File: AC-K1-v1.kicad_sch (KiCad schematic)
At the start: 169 parts, among them J1 S2B-PH-K-SLFSN, SW1 ESC, SW10 A, SW11 BSLH, SW12 LCMD, SW13 F2, SW14 2, SW15 W, SW16 S, SW17 Z, SW18 LALT, SW19 F3, SW2 GRAVE, SW20 3, SW21 E, SW22 D, SW23 X, SW24 F4, SW25 4, SW26 R, SW27 F, SW28 C, SW29 5, SW3 TAB, SW30 T, SW31 G, SW32 V, SW33 F5, SW34 6, SW35 Y, SW36 H, SW37 B, SW38 SPACE, SW39 F6, SW4 LCTRL, SW40 7, SW41 U, SW42 J, SW43 N, SW44 F7, SW45 8, SW46 I, SW47 K, SW48 M, SW49 F8, SW5 LSHIFT, SW50 9, SW51 O, SW52 L, SW53 COMMA, SW54 RALT, SW55 F9, SW56 0, SW57 P, SW58 SEMI, SW59 DOT, SW6 LCTRL, SW60 FN, SW61 F10, SW62 MINUS, SW63 LBKT, SW64 SQT, SW65 FSLH, SW66 RCTRL, SW67 F11, SW68 EQUAL, SW69 RBKT, SW7 F1, SW70 NUHS, SW71 RSHFT, SW72 LEFT, SW73 F12, SW74 BSPC, SW75 ENTER, SW76 UP, SW77 DOWN, SW78 DEL, SW79 HOME, SW8 1, SW80 PG_UP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

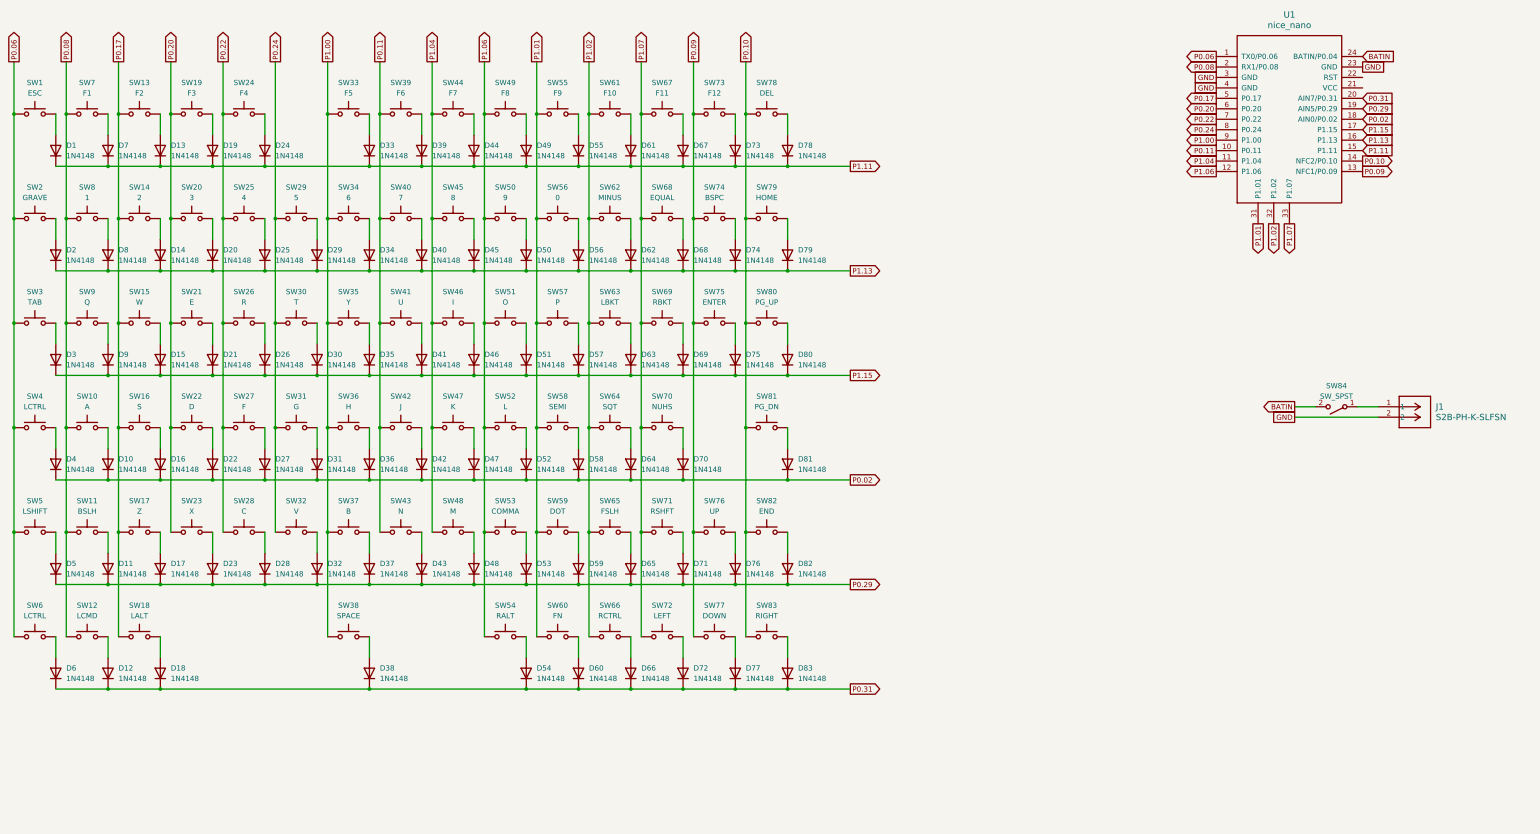
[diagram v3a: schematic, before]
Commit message: Added spacings to keycaps for easier alignment
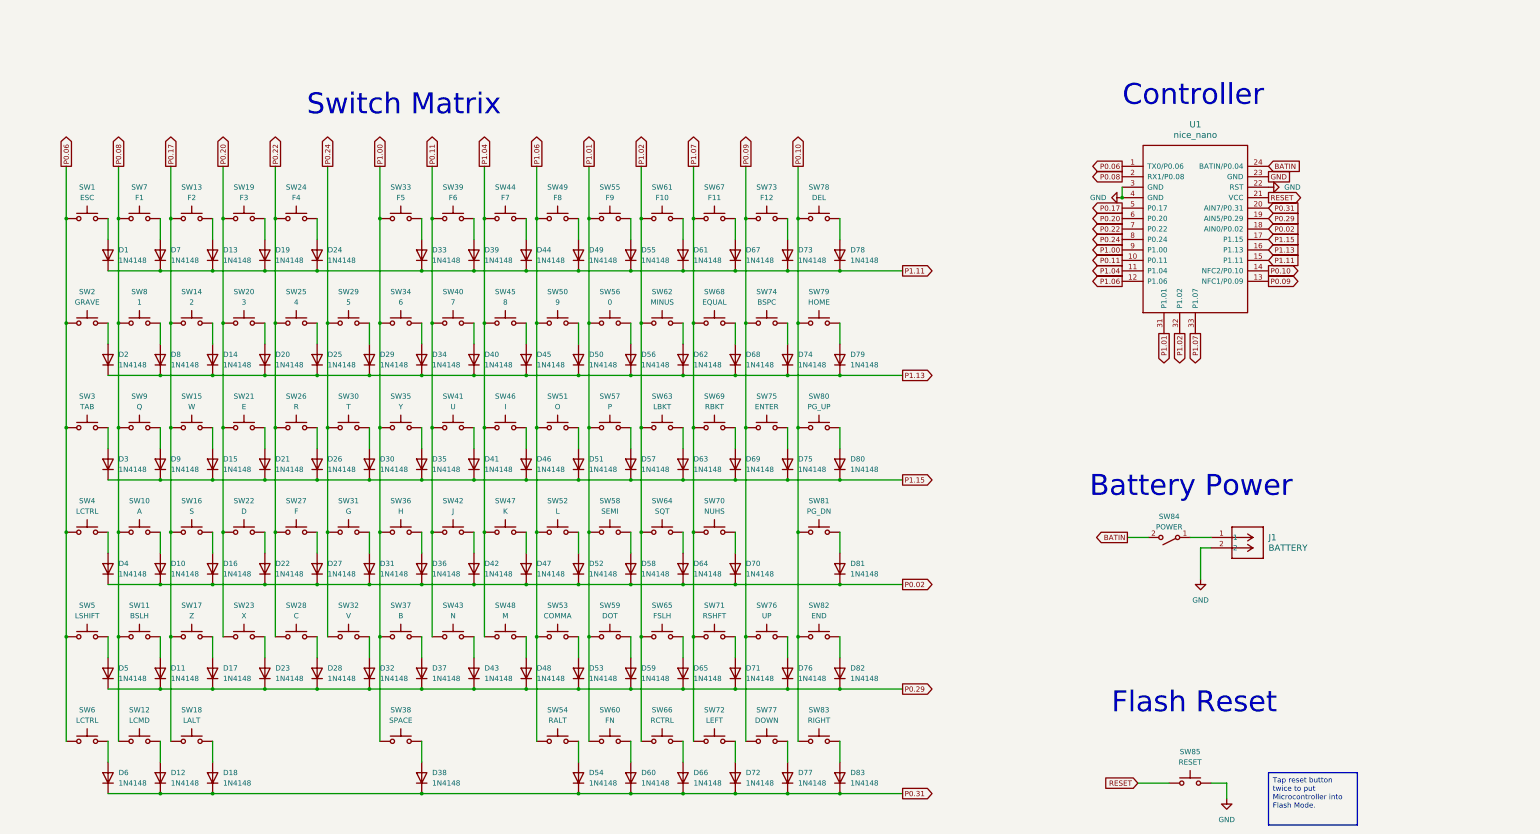
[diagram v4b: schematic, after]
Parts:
- added SW85: RESET, Button_Switch_THT:SW_PUSH_1P1T_6x3.5mm_H4.3_APEM_MJTP1243, symbol Switch:SW_Push
- J1: value S2B-PH-K-SLFSN -> BATTERY
- SW1, SW10, SW11, SW13, SW14, SW15, SW16, SW17, SW19, SW2, SW20, SW21, SW22, SW23, SW24, SW25, SW26, SW27, SW28, SW29, SW30, SW31, SW32, SW33, SW34, SW35, SW36, SW37, SW39, SW40, SW41, SW42, SW43, SW44, SW45, SW46, SW47, SW48, SW49, SW50, SW51, SW52, SW53, SW55, SW56, SW57, SW58, SW59, SW61, SW62, SW63, SW64, SW65, SW67, SW68, SW69, SW7, SW70, SW72, SW73, SW74, SW76, SW77, SW78, SW79, SW8, SW80, SW81, SW82, SW83, SW9: footprint marbastlib-choc:SW_choc_v1_1u -> Switch_Keyboard_Kailh:SW_Kailh_Choc_V1_1.00u_Spacing
- SW12, SW18, SW54, SW60, SW66: footprint marbastlib-choc:SW_choc_v1_1.25u -> Switch_Keyboard_Kailh:SW_Kailh_Choc_V1_1.25u_Spacing
- SW3: footprint marbastlib-choc:SW_choc_v1_1.5u -> Switch_Keyboard_Kailh:SW_Kailh_Choc_V1_1.50u_Spacing
- SW38: footprint Switch_Keyboard_Kailh:SW_Kailh_Choc_V1_6.00u -> Switch_Keyboard_Kailh:SW_Kailh_Choc_V1_6.00u_Spacing
- SW4: footprint marbastlib-choc:SW_choc_v1_1.75u -> Switch_Keyboard_Kailh:SW_Kailh_Choc_V1_1.75u_Spacing
- SW5, SW6: footprint marbastlib-choc:SW_choc_v1_1.25u -> Switch_Keyboard_Kailh:SW_Kailh_Choc_V1_1.50u_Spacing
- SW71: footprint marbastlib-choc:SW_choc_v1_1.75u -> Switch_Keyboard_Kailh:SW_Kailh_Choc_V1_1.00u_Spacing
- SW75: footprint Switch_Keyboard_Kailh:SW_Kailh_Choc_V1_ISOEnter -> Switch_Keyboard_Kailh:SW_Kailh_Choc_V1_ISOEnter_Spacing
- SW84: value SW_SPST -> POWER
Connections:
- net GND: now also U1.22 (RST), SW85.2
- net RESET: now reaches U1.21 (VCC)
- net RESET: now also SW85.1
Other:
- note added: "Battery Power"
- note added: "Controller"
- note added: "Flash Reset"
- note added: "Switch Matrix"
- moved on the sheet: D1, D10, D11, D12, D13, D14, D15, D16, D17, D18, D19, D2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

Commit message: Finished positioning switches
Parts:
- SW71: footprint Switch_Keyboard_Kailh:SW_Kailh_Choc_V1_1.00u_Spacing -> Switch_Keyboard_Kailh:SW_Kailh_Choc_V1_1.50u_Spacing
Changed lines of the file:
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@@
 			)
 		)
-		(property "Footprint" "Switch_Keyboard_Kailh:SW_Kailh_Choc_V1_1.00u_Spacing"
+		(property "Footprint" "Switch_Keyboard_Kailh:SW_Kailh_Choc_V1_1.50u_Spacing"
 			(at 208.28 172.72 0)
 			(effects

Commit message: Started pulling lanes
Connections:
- net GND: no longer U1.22 (RST)
- net RESET: now also U1.22 (RST); no longer U1.21 (VCC)
- no-connect marks 0 -> 1
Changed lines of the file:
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@@
 		(color 0 0 0 0)
 	)
+	(no_connect
+		(at 342.9 71.12)
+	)
 	(wire
 		(pts
@@
 	(global_label "RESET"
 		(shape output)
-		(at 342.9 71.12 0)
+		(at 342.9 68.58 0)
 		(fields_autoplaced yes)
 		(effects
@@
 		)
 		(property "Intersheetrefs" "${INTERSHEET_REFS}"
-			(at 351.6303 71.12 0)
+			(at 351.6303 68.58 0)
 			(effects
 				(font
@@
 		)
 	)
-	(global_label "GND"
-		(shape passive)
-		(at 342.9 66.04 0)
-		(fields_autoplaced yes)
-		(effects
-			(font
-				(size 1.27 1.27)
-			)
-			(justify left)
-		)
-		(property "Intersheetrefs" "${INTERSHEET_REFS}"
-			(at 348.6444 66.04 0)
-			(effects
-				(font
-					(size 1.27 1.27)
-				)
-				(justify left)
-				(hide yes)
-			)
-		)
-	)
 	(global_label "P0.06"
 		(shape output)
@@
 	(symbol
 		(lib_id "power:GND")
-		(at 342.9 68.58 90)
+		(at 342.9 66.04 90)
 		(unit 1)
 		(exclude_from_sim no)
@@
 		(fields_autoplaced yes)
 		(property "Reference" "#PWR02"
-			(at 349.25 68.58 0)
+			(at 349.25 66.04 0)
 			(effects
 				(font
@@
 		)
 		(property "Value" "GND"
-			(at 346.71 68.5799 90)
+			(at 346.71 66.0399 90)
 			(effects
 				(font
@@
 		)
 		(property "Footprint" ""
-			(at 342.9 68.58 0)
+			(at 342.9 66.04 0)
 			(effects
 				(font
@@
 		)
 		(property "Datasheet" ""
-			(at 342.9 68.58 0)
+			(at 342.9 66.04 0)
 			(effects
 				(font
@@
 		)
 		(property "Description" "Power symbol creates a global label with name \"GND\" , ground"
-			(at 342.9 68.58 0)
+			(at 342.9 66.04 0)
 			(effects
 				(font

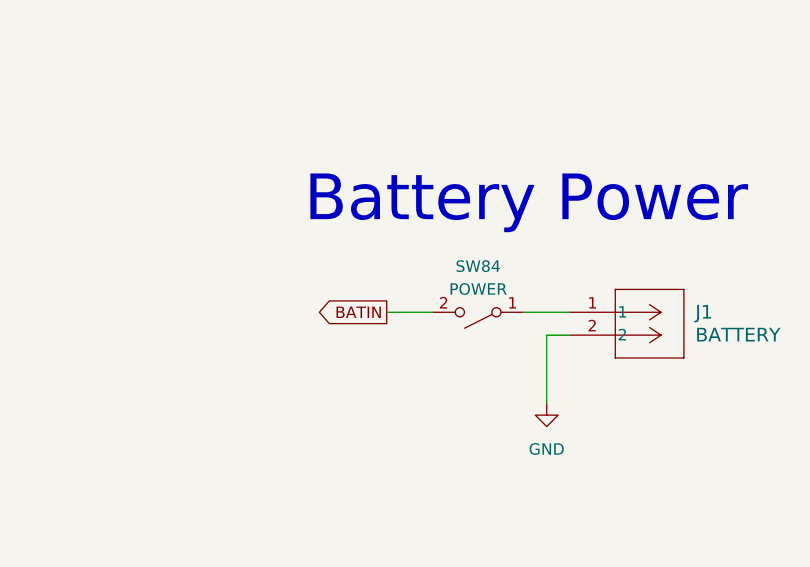
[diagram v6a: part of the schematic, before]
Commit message: Made Column traces
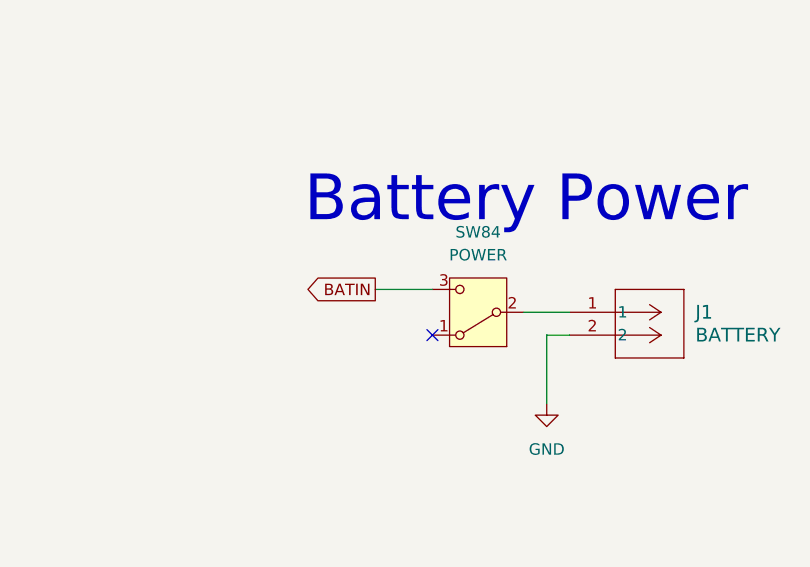
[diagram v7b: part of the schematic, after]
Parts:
- SW38: footprint Switch_Keyboard_Kailh:SW_Kailh_Choc_V1_6.00u_Spacing -> Switch_Keyboard_Kailh:SW_Kailh_Choc_V1_5.50u_Spacing
- SW84: symbol Switch:SW_SPST -> Switch:SW_SPDT
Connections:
- net BATIN: now also SW84.3 (C); no longer SW84.2 (B)
- net at SW84.1 (A): no longer J1.1
- new net: J1.1, SW84.2 (B)
- no-connect marks 1 -> 2
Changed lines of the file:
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@@
 		(at 342.9 71.12)
 	)
+	(no_connect
+		(at 313.69 156.21)
+	)
 	(wire
 		(pts
@@
 	(wire
 		(pts
-			(xy 308.61 153.67) (xy 313.69 153.67)
+			(xy 307.34 151.13) (xy 313.69 151.13)
 		)
 		(stroke
@@
 	(global_label "BATIN"
 		(shape output)
-		(at 308.61 153.67 180)
+		(at 307.34 151.13 180)
 		(fields_autoplaced yes)
 		(effects
@@
 		)
 		(property "Intersheetrefs" "${INTERSHEET_REFS}"
-			(at 300.3633 153.67 0)
+			(at 299.0933 151.13 0)
 			(effects
 				(font
@@
 	)
 	(symbol
-		(lib_id "Switch:SW_SPST")
+		(lib_id "Switch:SW_SPDT")
 		(at 318.77 153.67 180)
 		(unit 1)
@@
 		(fields_autoplaced yes)
 		(property "Reference" "SW84"
-			(at 318.77 148.59 0)
+			(at 318.77 144.78 0)
 			(effects
 				(font
@@
 		)
 		(property "Value" "POWER"
-			(at 318.77 151.13 0)
+			(at 318.77 147.32 0)
 			(effects
 				(font
@@
 		)
 		(property "Datasheet" "~"
-			(at 318.77 153.67 0)
+			(at 318.77 146.05 0)
 			(effects
 				(font
@@
 			)
 		)
-		(property "Description" "Single Pole Single Throw (SPST) switch"
+		(property "Description" "Switch, single pole double throw"
 			(at 318.77 153.67 0)
 			(effects
@@
 		(pin "1"
 		)
+		(pin "3"
+		)
 		(instances
 			(project "AC-K1-v1"
@@
 			)
 		)
-		(property "Footprint" "Switch_Keyboard_Kailh:SW_Kailh_Choc_V1_6.00u_Spacing"
+		(property "Footprint" "Switch_Keyboard_Kailh:SW_Kailh_Choc_V1_5.50u_Spacing"
 			(at 132.08 198.12 0)
 			(effects
